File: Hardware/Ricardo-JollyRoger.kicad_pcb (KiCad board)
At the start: 4 copper layers, 45.8 x 35.8 mm, 88 parts, among them J1 RBUS, J2 USB_C_Receptacle_USB2.0, J3 Conn_01x08_Pin, J4 Conn_01x02_Pin, U1 ESP32-S3, U2 SN65HVD230, U3 LM66200DRLR, U4 MAX77827AEFD+T, U5 SC4215ASTRT, U7 LM66200DRLR, Y1 R940000171

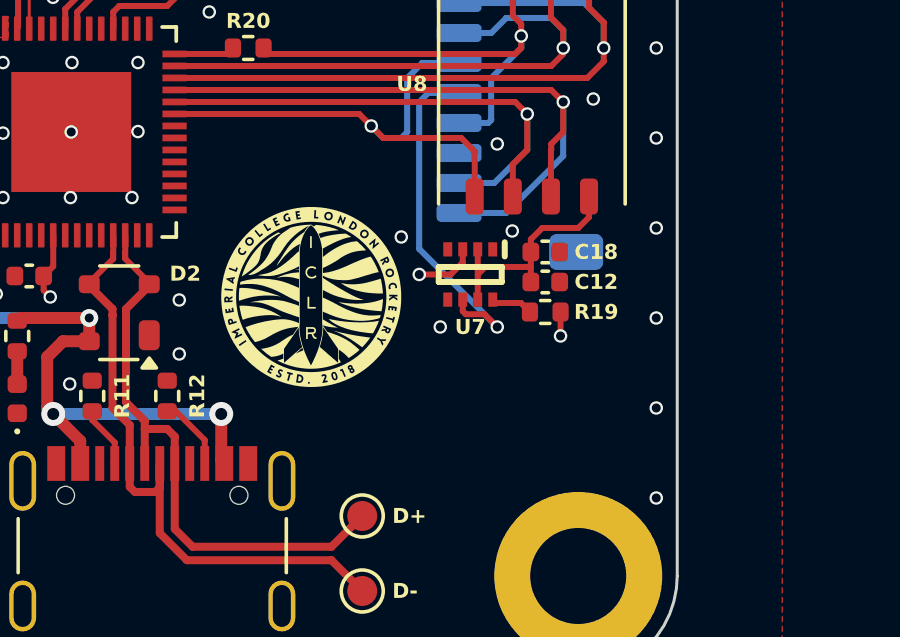
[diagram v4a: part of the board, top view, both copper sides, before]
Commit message: Add warning message
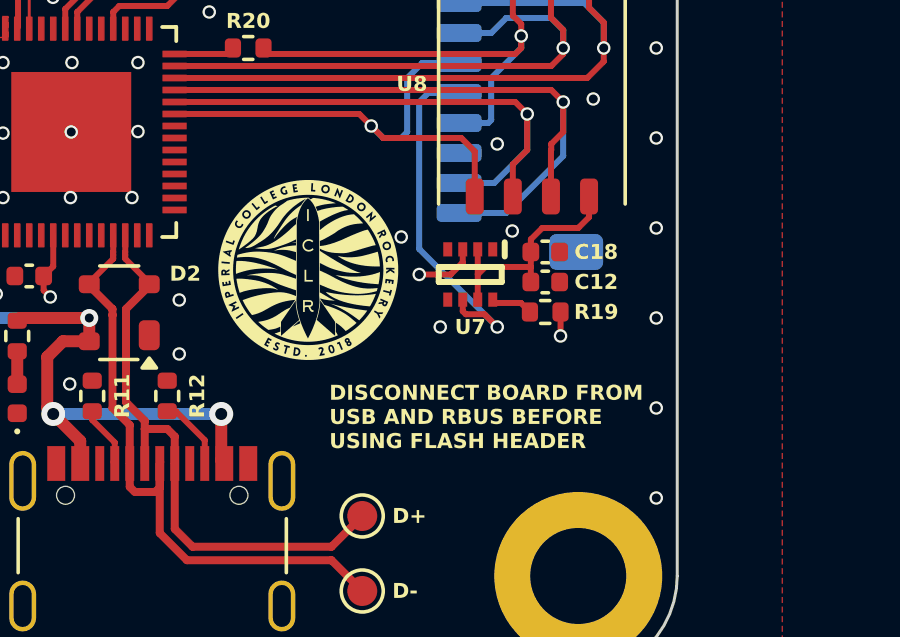
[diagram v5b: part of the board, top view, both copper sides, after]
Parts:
- moved G*** 0.91 mm to (112.6, 67.4)
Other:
- board text added: "DISCONNECT BOARD FROM USB AND RBUS BEFORE USING FLASH HEADER"
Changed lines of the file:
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@@
 			(layer "F.Mask"
 				(type "Top Solder Mask")
+				(color "Black")
 				(thickness 0.01)
 			)
@@
 			(layer "B.Mask"
 				(type "Bottom Solder Mask")
+				(color "Black")
 				(thickness 0.01)
 			)
@@
 	(footprint "iclr:iclr_logo_estd2018_6mm"
 		(layer "F.Cu")
-		(at 112.725 68.29)
+		(at 112.625 67.39)
 		(property "Reference" "G***"
 			(at 0 0 0)
@@
 		)
 	)
+	(gr_text "DISCONNECT BOARD FROM\nUSB AND RBUS BEFORE\nUSING FLASH HEADER"
+		(at 113.325 72.29 0)
+		(layer "F.SilkS")
+		(effects
+			(font
+				(size 0.5 0.5)
+				(thickness 0.1)
+				(bold yes)
+			)
+			(justify left)
+		)
+	)
 	(gr_text "TXD"
 		(at 109.025 56.09 0)
@@
 	)
 	(zone
+		(net 1)
+		(net_name "GND")
+		(layer "F.Cu")
+		(name "$teardrop_padvia$")
+		(hatch full 0.1)
+		(priority 30002)
+		(attr
+			(teardrop
+				(type padvia)
+			)
+		)
+		(connect_pads yes
+			(clearance 0)
+		)
+		(min_thickness 0.0254)
+		(filled_areas_thickness no)
+		(fill yes
+			(thermal_gap 0.5)
+			(thermal_bridge_width 0.5)
+			(island_removal_mode 1)
+			(island_area_min 10)
+		)
+		(polygon
+			(pts
+				(xy 88.316888 72.386882) (xy 88.566888 72.386882) (xy 88.649761 72.022986) (xy 88.441888 71.935882)
+				(xy 88.234015 72.022986)
+			)
+		)
+	)
+	(zone
 		(net 7)
 		(net_name "/Power/BBOUT")
@@
 	)
 	(zone
-		(net 3)
-		(net_name "VBUS")
+		(net 8)
+		(net_name "/Power/LX1")
 		(layer "F.Cu")
-		(name "$teardrop_padvia$")
-		(hatch full 0.1)
-		(priority 30001)
-		(attr
-			(teardrop
-				(type padvia)
-			)
-		)
+		(hatch edge 0.508)
+		(priority 5)
 		(connect_pads yes
 			(clearance 0)
 		)
-		(min_thickness 0.0254)
+		(min_thickness 0.254)
 		(filled_areas_thickness no)
 		(fill yes
-			(thermal_gap 0.5)
-			(thermal_bridge_width 0.5)
-			(island_removal_mode 1)
-			(island_area_min 10)
+			(thermal_gap 0.508)
+			(thermal_bridge_width 0.508)
+			(smoothing fillet)
+			(radius 0.1)
 		)
 		(polygon
 			(pts
-				(xy 88.274825 76.3) (xy 88.274825 75.9) (xy 88.065987 75.742783) (xy 87.905888 75.901882) (xy 87.820784 76.109755)
+				(xy 92.313167 74.02865) (xy 92.122888 74.326882) (xy 92.124419 74.641518) (xy 92.124885 74.641518)
+				(xy 92.126352 75.042916) (xy 90.947911 75.043916) (xy 90.947885 74.641518) (xy 91.765629 74.641518)
+				(xy 91.764888 74.365882) (xy 91.875888 74.125882) (xy 91.872888 73.853882) (xy 91.872749 73.821137)
+				(xy 92.303596 73.819625)
 			)
 		)
 	)
 	(zone
-		(net 1)
-		(net_name "GND")
+		(net 3)
+		(net_name "VBUS")
 		(layer "F.Cu")
 		(name "$teardrop_padvia$")
 		(hatch full 0.1)
-		(priority 30002)
+		(priority 30001)
 		(attr
 			(teardrop
@@
 		(polygon
 			(pts
-				(xy 88.316888 72.386882) (xy 88.566888 72.386882) (xy 88.649761 72.022986) (xy 88.441888 71.935882)
-				(xy 88.234015 72.022986)
-			)
-		)
-	)
-	(zone
-		(net 8)
-		(net_name "/Power/LX1")
-		(layer "F.Cu")
-		(hatch edge 0.508)
-		(priority 5)
-		(connect_pads yes
-			(clearance 0)
-		)
-		(min_thickness 0.254)
-		(filled_areas_thickness no)
-		(fill yes
-			(thermal_gap 0.508)
-			(thermal_bridge_width 0.508)
-			(smoothing fillet)
-			(radius 0.1)
-		)
-		(polygon
-			(pts
-				(xy 92.313167 74.02865) (xy 92.122888 74.326882) (xy 92.124419 74.641518) (xy 92.124885 74.641518)
-				(xy 92.126352 75.042916) (xy 90.947911 75.043916) (xy 90.947885 74.641518) (xy 91.765629 74.641518)
-				(xy 91.764888 74.365882) (xy 91.875888 74.125882) (xy 91.872888 73.853882) (xy 91.872749 73.821137)
-				(xy 92.303596 73.819625)
+				(xy 88.274825 76.3) (xy 88.274825 75.9) (xy 88.065987 75.742783) (xy 87.905888 75.901882) (xy 87.820784 76.109755)
 			)
 		)
@@
 		(name "$teardrop_padvia$")
 		(hatch full 0.1)
-		(priority 30001)
+		(priority 30000)
 		(attr
 			(teardrop
@@
 		(polygon
 			(pts
-				(xy 87.984619 71.413224) (xy 87.701776 71.130381) (xy 87.365901 71.430901) (xy 87.524293 71.590707)
-				(xy 87.684099 71.749099)
+				(xy 87.325 72.04) (xy 87.725 72.04) (xy 87.75 71.59) (xy 87.525 71.589) (xy 87.3 71.59)
 			)
 		)
@@
 	)
 	(zone
-		(net 1)
-		(net_name "GND")
-		(layer "B.Cu")
-		(hatch edge 0.5)
-		(priority 1)
-		(connect_pads yes
-			(clearance 0)
-		)
-		(min_thickness 0.25)
-		(filled_areas_thickness no)
-		(fill yes
-			(thermal_gap 0.5)
-			(thermal_bridge_width 0.5)
-		)
-		(polygon
-			(pts
-				(xy 135.925 35.59) (xy 135.925 90.59) (xy 65.925 90.59) (xy 65.925 35.59)
-			)
-		)
-	)
-	(zone
 		(net 3)
 		(net_name "VBUS")
@@
 		(name "$teardrop_padvia$")
 		(hatch full 0.1)
-		(priority 30000)
+		(priority 30001)
 		(attr
 			(teardrop
@@
 		(polygon
 			(pts
-				(xy 87.325 72.04) (xy 87.725 72.04) (xy 87.75 71.59) (xy 87.525 71.589) (xy 87.3 71.59)
+				(xy 87.984619 71.413224) (xy 87.701776 71.130381) (xy 87.365901 71.430901) (xy 87.524293 71.590707)
+				(xy 87.684099 71.749099)
 			)
 		)
@@
 			)
 		)
+	)
+	(zone
+		(net 1)
+		(net_name "GND")
+		(layer "B.Cu")
+		(hatch edge 0.5)
+		(priority 1)
+		(connect_pads yes
+			(clearance 0)
+		)
+		(min_thickness 0.25)
+		(filled_areas_thickness no)
+		(fill yes
+			(thermal_gap 0.5)
+			(thermal_bridge_width 0.5)
+		)
+		(polygon
+			(pts
+				(xy 135.925 35.59) (xy 135.925 90.59) (xy 65.925 90.59) (xy 65.925 35.59)
+			)
+		)

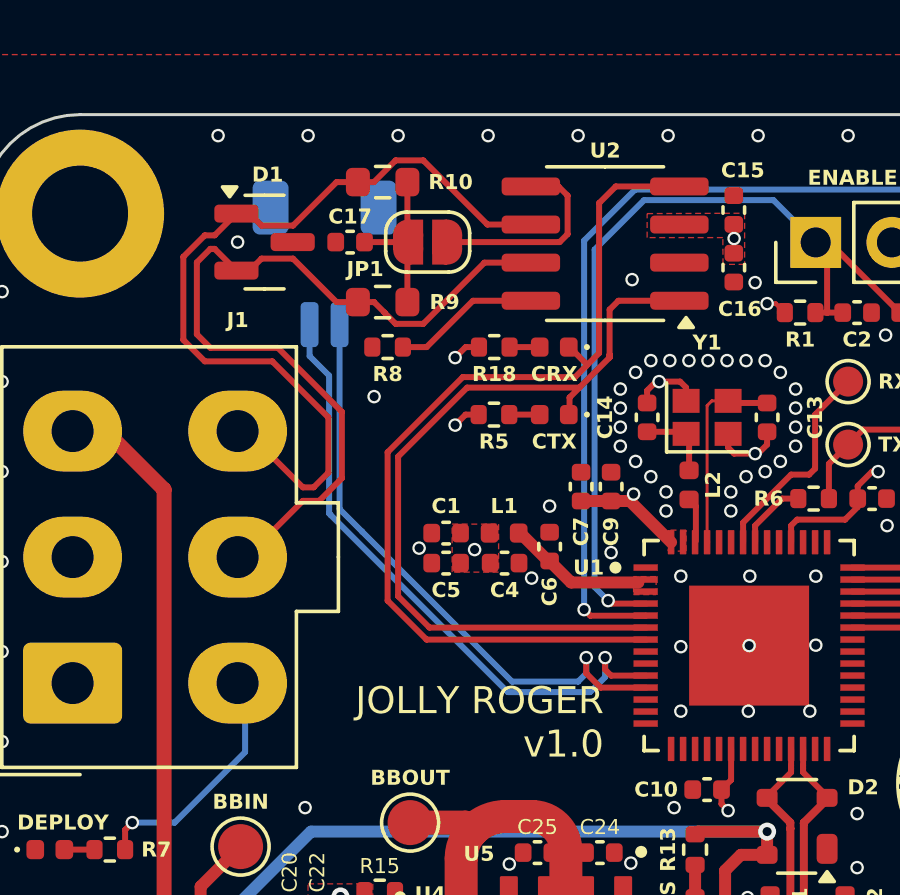
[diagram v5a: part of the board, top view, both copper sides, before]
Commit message: Upgrade GPIO breakout to four pins
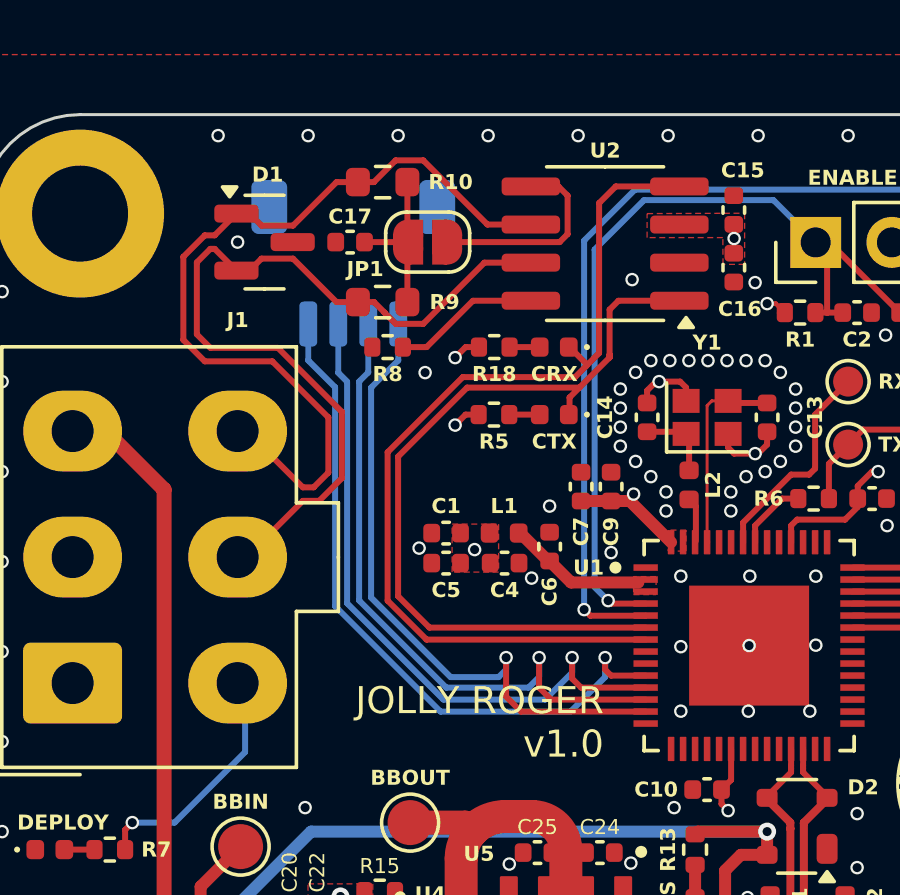
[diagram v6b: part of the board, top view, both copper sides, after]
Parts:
- J4: footprint Connector_Molex:Molex_Pico-Clasp_202396-0207_1x02-1MP_P1.00mm_Horizontal -> Connector_Molex:Molex_Pico-Clasp_202396-0407_1x04-1MP_P1.00mm_Horizontal
- moved J4 0.96 mm to (91.5, 50.0)
- moved REF** 0.50 mm to (103.1, 63.7)
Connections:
- U1 pad 12: unconnected-(U1-GPIO7/ADC1_CH6-Pad12) -> /GPIO7
- U1 pad 13: unconnected-(U1-GPIO8/ADC1_CH7-Pad13) -> /GPIO8
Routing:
- net /GPIO7: track 0.00 -> 22.1 mm, vias 0 -> 1
- net /GPIO8: track 0.00 -> 21.8 mm, vias 0 -> 1
- net /GPIO6: track 20.1 -> 22.4 mm
- net /GPIO5: track 20.9 -> 23.2 mm
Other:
- board text added: "GPIO7"
- board text added: "GPIO8"

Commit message: Added 3V3 and GND to GPIO breakout
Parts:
- J4: value Conn_01x02_Pin -> Conn_01x06_Pin; footprint Connector_Molex:Molex_Pico-Clasp_202396-0407_1x04-1MP_P1.00mm_Horizontal -> Connector_Molex:Molex_Pico-Clasp_202396-0607_1x06-1MP_P1.00mm_Horizontal
- moved J4 1.00 mm to (92.5, 50.0)
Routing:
- net +3V3: track 24.5 -> 28.5 mm
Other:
- board text added: "3V3"
- board text added: "GND"

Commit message: Updated NAND flash symbol
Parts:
- U8: value ~ -> ZDSD04GLGEAG
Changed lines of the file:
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@@
 			)
 		)
-		(property "Value" "~"
+		(property "Value" "ZDSD04GLGEAG"
 			(at 0 3.95 90)
 			(layer "F.Fab")
@@
 			)
 		)
-		(property "Datasheet" ""
+		(property "Datasheet" "https://www.lcsc.com/datasheet/lcsc_datasheet_2410010101_Zetta-ZDSD04GLGEAG_C2875854.pdf"
 			(at 0 0 -90)
 			(unlocked yes)
